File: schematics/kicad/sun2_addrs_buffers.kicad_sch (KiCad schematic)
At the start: 0 parts

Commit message: work on addresses and buffers
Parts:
- added U1, U2, U3, U4, U5, U6: 74LS533, Package_DIP:DIP-20_W7.62mm, symbol sun2:74LS533
- added U101: 74F32, Package_DIP:DIP-14_W7.62mm, symbol sun2:74F32
- added U102: 74F00, Package_DIP:DIP-14_W7.62mm, symbol sun2:74F00
- added U7, U8, U9: 8303, Package_DIP:DIP-20_W7.62mm, symbol sun2:8303
- added U703: 74F08, Package_DIP:DIP-14_W7.62mm, symbol sun2:74F08

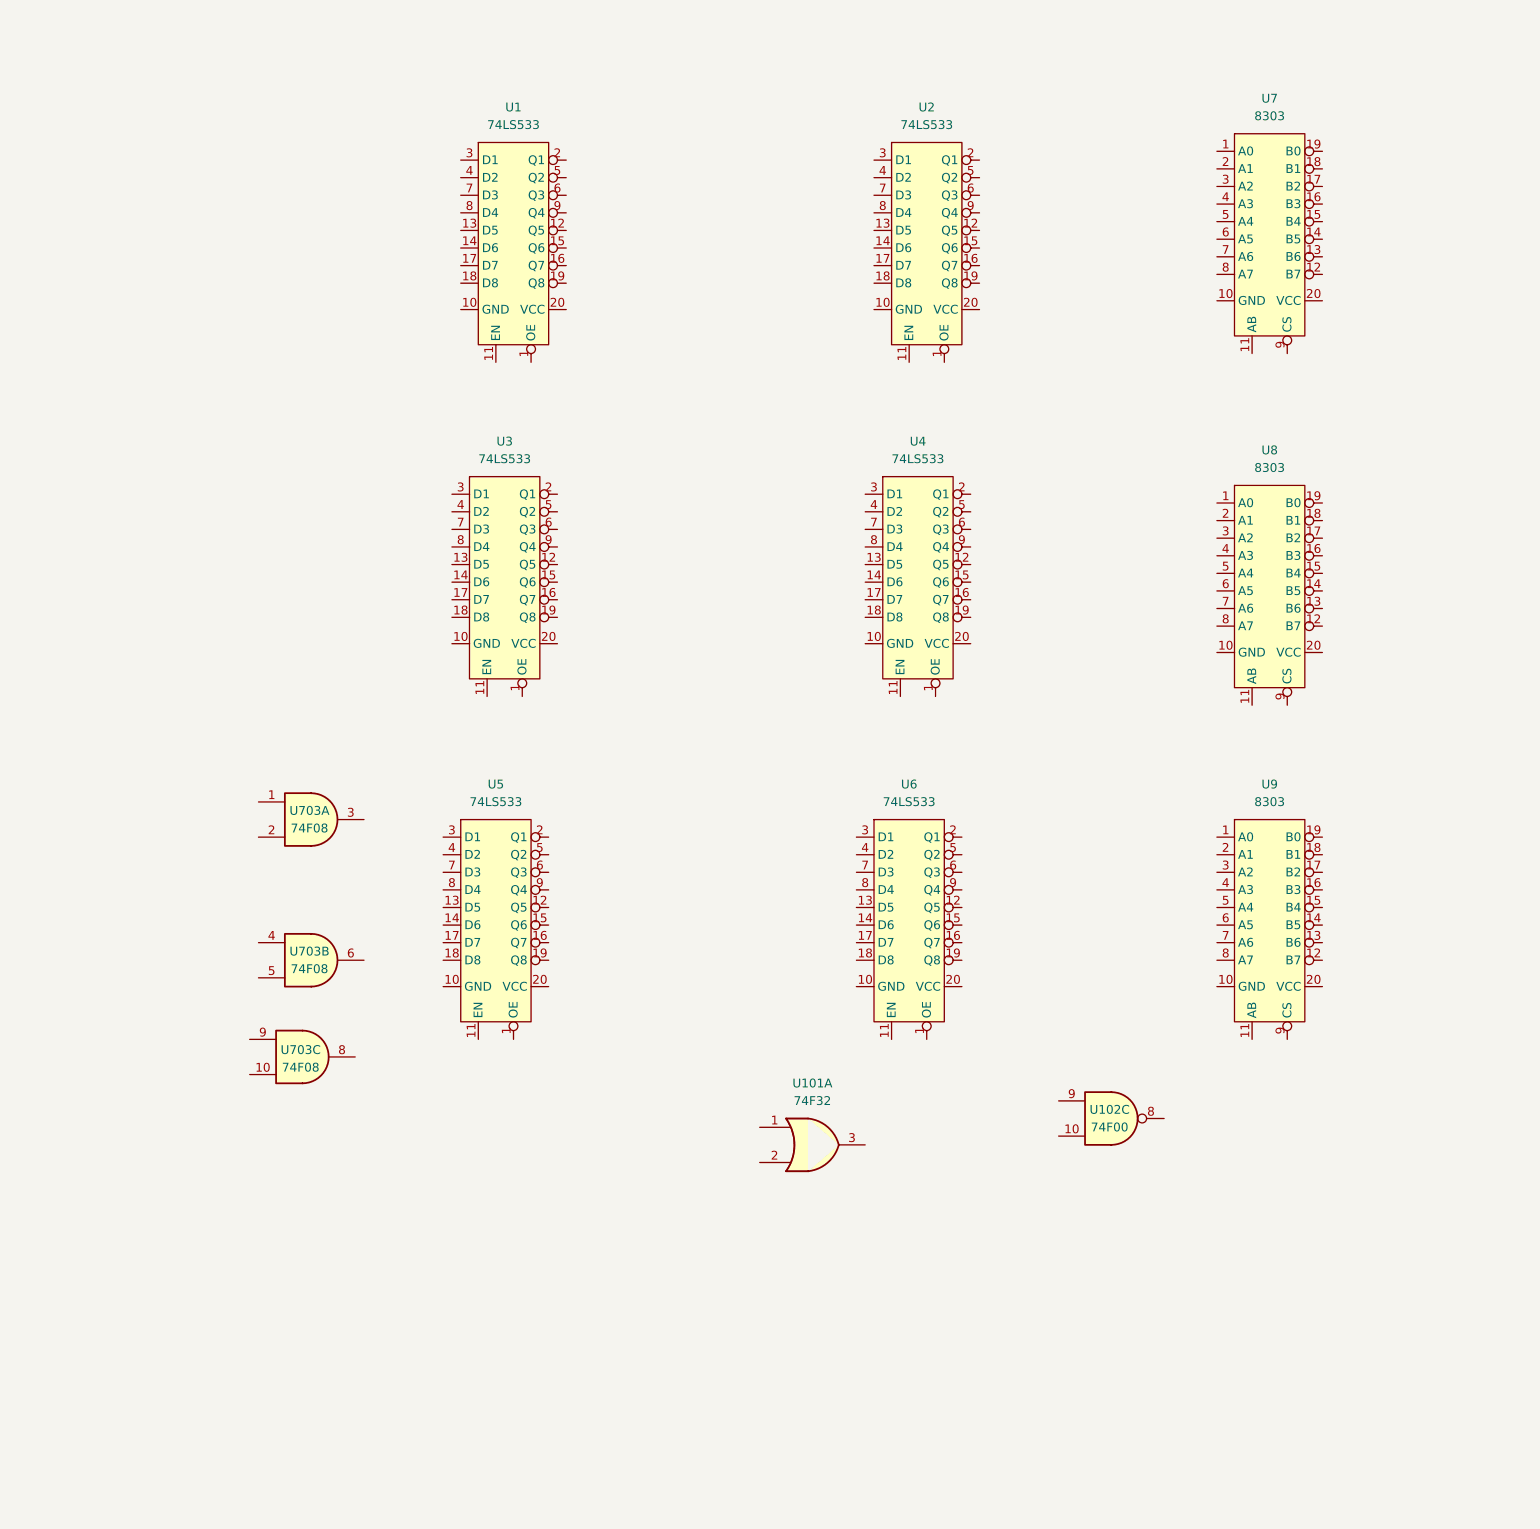
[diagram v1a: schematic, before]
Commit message: Finish address in/out and data buffers
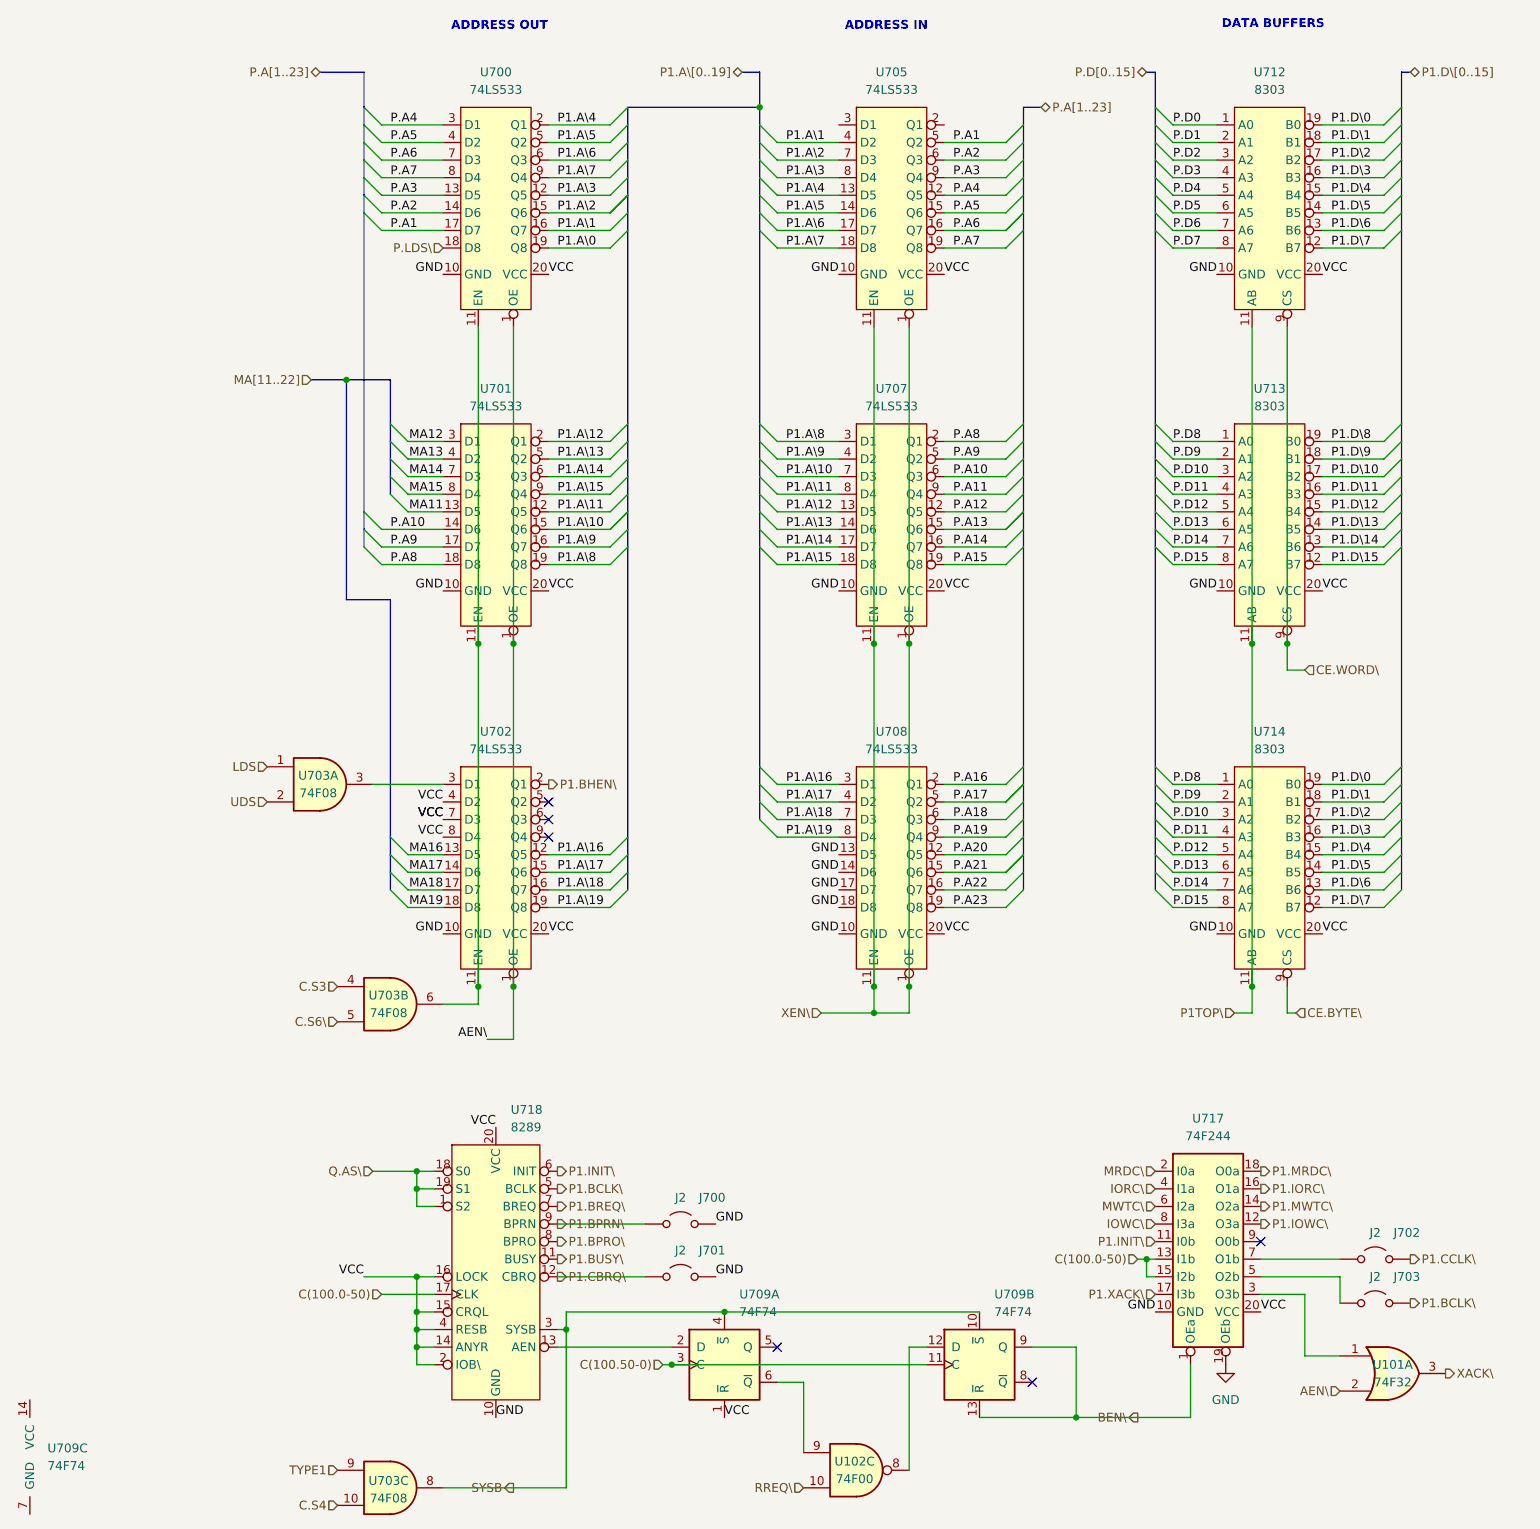
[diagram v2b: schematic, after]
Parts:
- added J700, J701, J702, J703: J2, TestPoint:TestPoint_2Pads_Pitch2.54mm_Drill0.8mm, symbol Jumper:Jumper_2_Open
- added U709: 74F74, Package_DIP:DIP-14_W7.62mm, symbol sun2:74F74
- added U717: 74F244, Package_DIP:DIP-20_W7.62mm, symbol sun2:74F244
- added U718: 8289, Package_DIP:DIP-20_W7.62mm, symbol sun2:8289
- renumbered U1 to U700, U3 to U701, U5 to U702, U2 to U705, U4 to U707, U6 to U708, U7 to U712, U8 to U713, U9 to U714
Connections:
- net at U101.1: now also U717.3 (O3b)
- net AEN\: now reaches U101.2
- net AEN\: now also U700.1 (OE), U701.1 (OE), U702.1 (OE)
- net XACK\: now reaches U101.3
- net P.D8: now reaches U713.1 (A0)
- net P.D8: now also U714.1 (A0)
- net GND: now reaches U713.10 (GND)
- net GND: now also U700.10 (GND), U701.10 (GND), U702.10 (GND), U705.10 (GND), U707.10 (GND), U708.10 (GND), U708.13 (D5), U708.14 (D6), U708.17 (D7), U708.18 (D8), U712.10 (GND), U714.10 (GND), J700.2 (B), J701.2 (B), U717.10 (GND), U717.19 (OEb), U718.10 (GND)
- net P1TOP\: now reaches U713.11 (AB)
- net P1TOP\: now also U712.11 (AB), U714.11 (AB)
- net P1.D\15: now reaches U713.12 (B7)
- net P1.D\14: now reaches U713.13 (B6)
- net P1.D\13: now reaches U713.14 (B5)
- net P1.D\12: now reaches U713.15 (B4)
- net P1.D\11: now reaches U713.16 (B3)
- net P1.D\10: now reaches U713.17 (B2)
- net P1.D\9: now reaches U713.18 (B1)
- net P1.D\8: now reaches U713.19 (B0)
- net P.D9: now reaches U713.2 (A1)
- net P.D9: now also U714.2 (A1)
- net VCC: now reaches U713.20 (VCC)
- net VCC: now also U700.20 (VCC), U701.20 (VCC), U702.20 (VCC), U702.4 (D2), U702.7 (D3), U702.8 (D4), U705.20 (VCC), U707.20 (VCC), U708.20 (VCC), U712.20 (VCC), U714.20 (VCC), U709.1 (~{R}), U717.20 (VCC), U718.14 (ANYR), U718.15 (CRQL), U718.16 (LOCK), U718.2 (IOB\), U718.20 (VCC), U718.4 (RESB)
- net P.D10: now reaches U713.3 (A2)
- net P.D10: now also U714.3 (A2)
- net P.D11: now reaches U713.4 (A3)
- net P.D11: now also U714.4 (A3)
- net P.D12: now reaches U713.5 (A4)
- net P.D12: now also U714.5 (A4)
- net P.D13: now reaches U713.6 (A5)
- net P.D13: now also U714.6 (A5)
- net P.D14: now reaches U713.7 (A6)
- net P.D14: now also U714.7 (A6)
- net P.D15: now reaches U713.8 (A7)
- net P.D15: now also U714.8 (A7)
- net CE.WORD\: now reaches U713.9 (CS)
- net CE.WORD\: now also U712.9 (CS)
- net P.D0: now reaches U712.1 (A0)
- net P1.D\7: now reaches U712.12 (B7)
- net P1.D\7: now also U714.12 (B7)
- net P1.D\6: now reaches U712.13 (B6)
- net P1.D\6: now also U714.13 (B6)
- net P1.D\5: now reaches U712.14 (B5)
- net P1.D\5: now also U714.14 (B5)
- net P1.D\4: now reaches U712.15 (B4)
- net P1.D\4: now also U714.15 (B4)
- net P1.D\3: now reaches U712.16 (B3)
- net P1.D\3: now also U714.16 (B3)
- net P1.D\2: now reaches U712.17 (B2)
- net P1.D\2: now also U714.17 (B2)
- net P1.D\1: now reaches U712.18 (B1)
- net P1.D\1: now also U714.18 (B1)
- net P1.D\0: now reaches U712.19 (B0)
- net P1.D\0: now also U714.19 (B0)
- net P.D1: now reaches U712.2 (A1)
- net P.D2: now reaches U712.3 (A2)
- net P.D3: now reaches U712.4 (A3)
- net P.D4: now reaches U712.5 (A4)
- net P.D5: now reaches U712.6 (A5)
- net P.D6: now reaches U712.7 (A6)
- net P.D7: now reaches U712.8 (A7)
- net CE.BYTE\: now reaches U714.9 (CS)
- net RREQ\: now reaches U102.10
- net at U102.8: now also U709.12 (D)
- net at U102.9: now also U709.6 (~{Q})
- net LDS: now reaches U703.1
- net UDS: now reaches U703.2
- net at U703.3: now also U702.3 (D1)
- net at U701.11 (EN): now also U700.11 (EN), U702.11 (EN), U703.6
- net P1.A\11: now reaches U701.12 (Q5)
- net P1.A\11: now also U707.8 (D4)
- net MA11: now reaches U701.13 (D5)
- net P.A10: now reaches U701.14 (D6)
- net P.A10: now also U707.6 (Q3)
- net P1.A\10: now reaches U701.15 (Q6)
- net P1.A\10: now also U707.7 (D3)
- net P1.A\9: now reaches U701.16 (Q7)
- net P1.A\9: now also U707.4 (D2)
- net P.A9: now reaches U701.17 (D7)
- net P.A9: now also U707.5 (Q2)
- net P.A8: now reaches U701.18 (D8)
- net P.A8: now also U707.2 (Q1)
- net P1.A\8: now reaches U701.19 (Q8)
- net P1.A\8: now also U707.3 (D1)
- net P1.A\12: now reaches U701.2 (Q1)
- net P1.A\12: now also U707.13 (D5)
- net MA12: now reaches U701.3 (D1)
- net MA13: now reaches U701.4 (D2)
- net P1.A\13: now reaches U701.5 (Q2)
- net P1.A\13: now also U707.14 (D6)
- net P1.A\14: now reaches U701.6 (Q3)
- net P1.A\14: now also U707.17 (D7)
- net MA14: now reaches U701.7 (D3)
- net MA15: now reaches U701.8 (D4)
- net P1.A\15: now reaches U701.9 (Q4)
- net P1.A\15: now also U707.18 (D8)
- net C.S3: now reaches U703.4
- net C.S6\: now reaches U703.5
- net C.S4: now reaches U703.10
- net SYSB: now reaches U703.8
- net SYSB: now also U709.10 (~{S}), U709.4 (~{S}), U718.3 (SYSB)
- net TYPE1: now reaches U703.9
- net P1.A\16: now reaches U702.12 (Q5)
- net P1.A\16: now also U708.3 (D1)
- net MA16: now reaches U702.13 (D5)
- net MA17: now reaches U702.14 (D6)
- net P1.A\17: now reaches U702.15 (Q6)
- net P1.A\17: now also U708.4 (D2)
- net P1.A\18: now reaches U702.16 (Q7)
- net P1.A\18: now also U708.7 (D3)
- net MA18: now reaches U702.17 (D7)
- net MA19: now reaches U702.18 (D8)
- net P1.A\19: now reaches U702.19 (Q8)
- net P1.A\19: now also U708.8 (D4)
- net P1.BHEN\: now reaches U702.2 (Q1)
- net XEN\: now reaches U707.1 (OE)
- net XEN\: now also U705.1 (OE), U705.11 (EN), U707.11 (EN), U708.1 (OE), U708.11 (EN)
- net P.A12: now reaches U707.12 (Q5)
- net P.A13: now reaches U707.15 (Q6)
- net P.A14: now reaches U707.16 (Q7)
- net P.A15: now reaches U707.19 (Q8)
- net P.A11: now reaches U707.9 (Q4)
- net P.A4: now reaches U705.12 (Q5)
- net P.A4: now also U700.3 (D1)
- net P1.A\4: now reaches U705.13 (D5)
- net P1.A\4: now also U700.2 (Q1)
- net P1.A\5: now reaches U705.14 (D6)
- net P1.A\5: now also U700.5 (Q2)
- net P.A5: now reaches U705.15 (Q6)
- net P.A5: now also U700.4 (D2)
- net P.A6: now reaches U705.16 (Q7)
- net P.A6: now also U700.7 (D3)
- net P1.A\6: now reaches U705.17 (D7)
- net P1.A\6: now also U700.6 (Q3)
- net P1.A\7: now reaches U705.18 (D8)
- net P1.A\7: now also U700.9 (Q4)
- net P.A7: now reaches U705.19 (Q8)
- net P.A7: now also U700.8 (D4)
- net P1.A\1: now reaches U705.4 (D2)
- net P1.A\1: now also U700.16 (Q7)
- net P.A1: now reaches U705.5 (Q2)
- net P.A1: now also U700.17 (D7)
- net P.A2: now reaches U705.6 (Q3)
- net P.A2: now also U700.14 (D6)
- net P1.A\2: now reaches U705.7 (D3)
- net P1.A\2: now also U700.15 (Q6)
- net P1.A\3: now reaches U705.8 (D4)
- net P1.A\3: now also U700.12 (Q5)
- net P.A3: now reaches U705.9 (Q4)
- net P.A3: now also U700.13 (D5)
- net P.A20: now reaches U708.12 (Q5)
- net P.A21: now reaches U708.15 (Q6)
- net P.A22: now reaches U708.16 (Q7)
- net P.A23: now reaches U708.19 (Q8)
- net P.A16: now reaches U708.2 (Q1)
- net P.A17: now reaches U708.5 (Q2)
- net P.A18: now reaches U708.6 (Q3)
- net P.A19: now reaches U708.9 (Q4)
- net P.LDS\: now reaches U700.18 (D8)
- net P1.A\0: now reaches U700.19 (Q8)
- new net: J703.1 (A), U717.5 (O2b)
- new net: U709.2 (D), U718.13 (AEN)
- new net: J702.1 (A), U717.7 (O1b)
- new net BEN\: U709.13 (~{R}), U709.9 (Q), U717.1 (OEa)
- new net C(100.0-50): U717.13 (I1b), U717.15 (I2b), U718.17 (CLK)
- new net C(100.50-0): U709.11 (C), U709.3 (C)
- new net IORC\: U717.4 (I1a)
- new net IOWC\: U717.8 (I3a)
- new net MRDC\: U717.2 (I0a)
- new net MWTC\: U717.6 (I2a)
- new net P1.BCLK\: J703.2 (B), U718.5 (BCLK)
- new net P1.BPRN\: J700.1 (A), U718.9 (BPRN)
- new net P1.BPRO\: U718.8 (BPRO)
- new net P1.BREQ\: U718.7 (BREQ)
- new net P1.BUSY\: U718.11 (BUSY)
- new net P1.CBRQ\: J701.1 (A), U718.12 (CBRQ)
- new net P1.CCLK\: J702.2 (B)
- new net P1.INIT\: U717.11 (I0b), U718.6 (INIT)
- new net P1.IORC\: U717.16 (O1a)
- new net P1.IOWC\: U717.12 (O3a)
- new net P1.MRDC\: U717.18 (O0a)
- new net P1.MWTC\: U717.14 (O2a)
- new net P1.XACK\: U717.17 (I3b)
- new net Q.AS\: U718.1 (S2), U718.18 (S0), U718.19 (S1)
- no-connect marks 0 -> 6
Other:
- note added: "ADDRESS IN"
- note added: "ADDRESS OUT"
- note added: "DATA BUFFERS"
- moved on the sheet: U101A, U102C, U700, U701, U702, U703A, U703B, U703C, U705, U707, U708, U712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

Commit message: Finish passives
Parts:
- removed unit 3 of U709
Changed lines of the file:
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@@
-	)
-	(symbol
-		(lib_id "sun2:74F74")
-		(at -12.7 224.79 0)
-		(unit 3)
-		(exclude_from_sim no)
-		(in_bom yes)
-		(on_board yes)
-		(dnp no)
-		(fields_autoplaced yes)
-		(property "Reference" "U709"
-			(at -10.16 224.1549 0)
-			(effects
-				(font
-					(size 1.27 1.27)
-				)
-				(justify left)
-			)
-		)
-		(property "Value" "74F74"
-			(at -10.16 226.6949 0)
-			(effects
-				(font
-					(size 1.27 1.27)
-				)
-				(justify left)
-			)
-		)
-		(property "Footprint" "Package_DIP:DIP-14_W7.62mm"
-			(at -12.7 224.79 0)
-			(effects
-				(font
-					(size 1.27 1.27)
-				)
-				(hide yes)
-			)
-		)
-		(property "Datasheet" "https://www.ti.com/lit/ds/symlink/sn74f74.pdf"
-			(at -12.7 224.79 0)
-			(effects
-				(font
-					(size 1.27 1.27)
-				)
-				(hide yes)
-			)
-		)
-		(property "Description" "Dual D Flip-flop, Set & Reset"
-			(at -12.7 224.79 0)
-			(effects
-				(font
-					(size 1.27 1.27)
-				)
-				(hide yes)
-			)
-		)
-		(property "Order Link" "https://www.digikey.com/en/products/detail/texas-instruments/SN74F74N/277204"
-			(at -12.7 224.79 0)
-			(effects
-				(font
-					(size 1.27 1.27)
-				)
-				(hide yes)
-			)
-		)
-		(pin "5"
-		)
-		(pin "14"
-		)
-		(pin "6"
-		)
-		(pin "4"
-		)
-		(pin "10"
-		)
-		(pin "3"
-		)
-		(pin "8"
-		)
-		(pin "7"
-		)
-		(pin "13"
-		)
-		(pin "9"
-		)
-		(pin "2"
-		)
-		(pin "12"
-		)
-		(pin "11"
-		)
-		(pin "1"
-		)
-		(instances
-			(project ""
-				(path "/67ee2072-0b57-4a50-8537-b17b5f651e89/7153c171-e6a5-40f1-bd07-288a1f1a2f2f"
-					(reference "U709")
-					(unit 3)
-				)
-			)
-		)
 	)
 	(symbol

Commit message: Start global connections, error fixes
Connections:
- net GND: now also U705.3 (D1)
- net P.FC2: now reaches U705.2 (Q1)
